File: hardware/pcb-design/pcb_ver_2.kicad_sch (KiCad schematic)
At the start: 28 parts, among them J1 GTFP08441BEU, J2 Conn_01x04_Pin, J3 USB4085-GF-A_REVA4, J4 Conn_01x07_Socket, J5 Screw_Terminal_01x02, J6 UART, Q1 NMOS, U1 ESP32-S3-WROOM-2, U2 LM1117MP-3.3

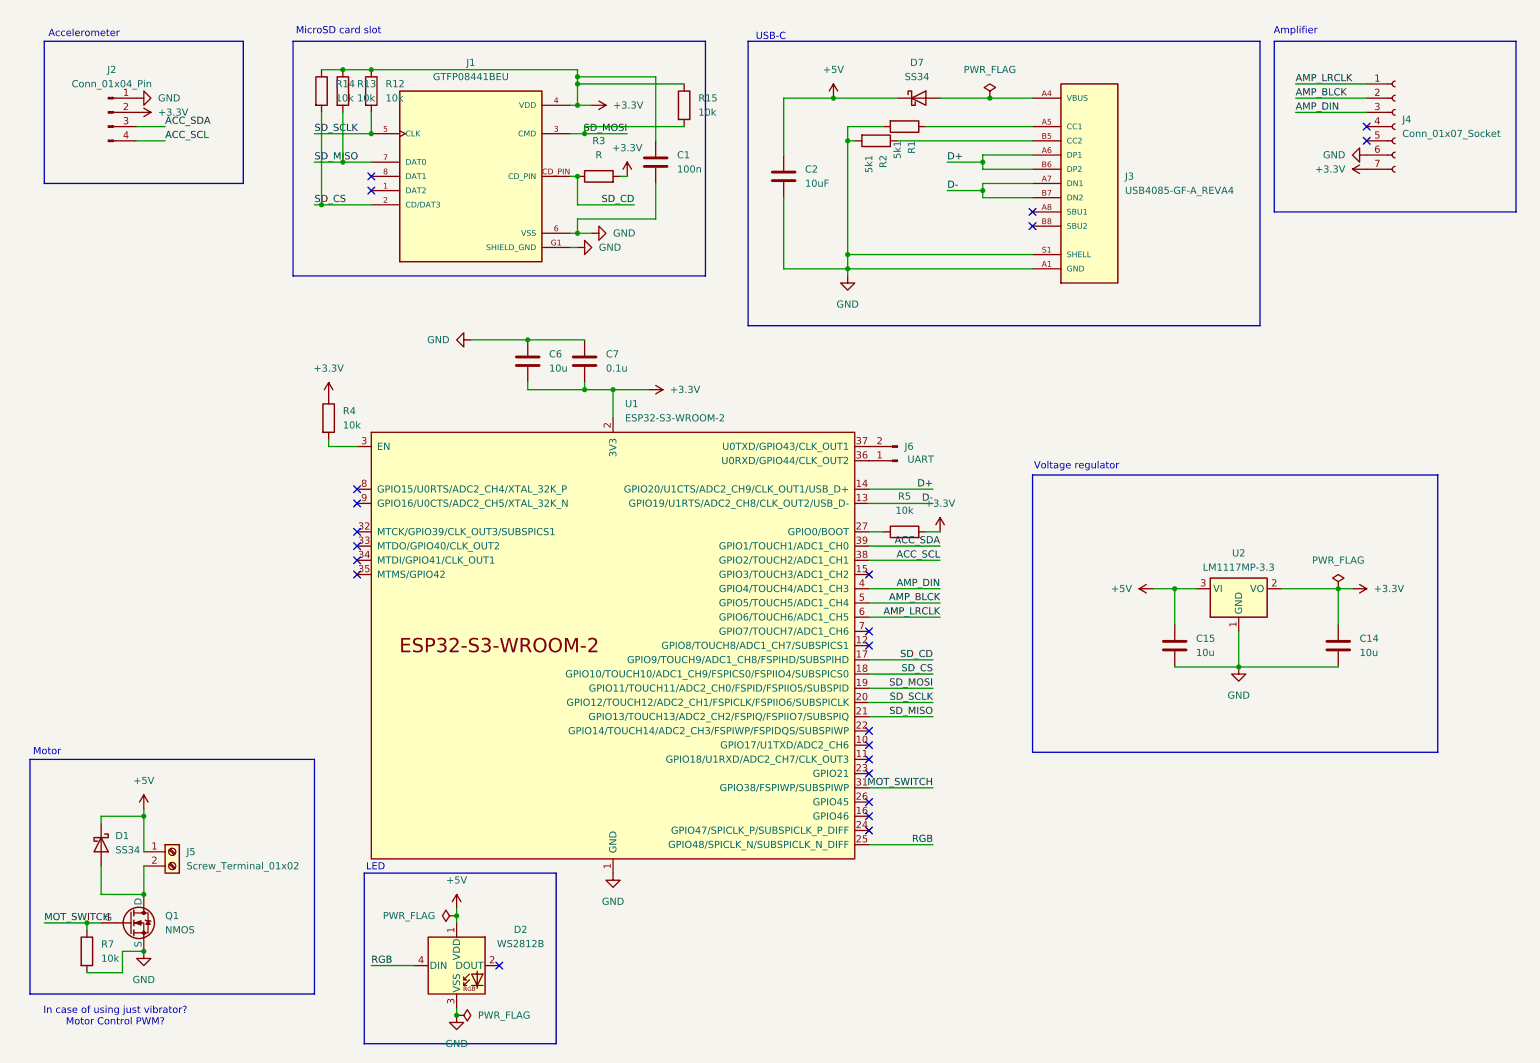
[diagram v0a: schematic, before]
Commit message: hardware: change to USB board
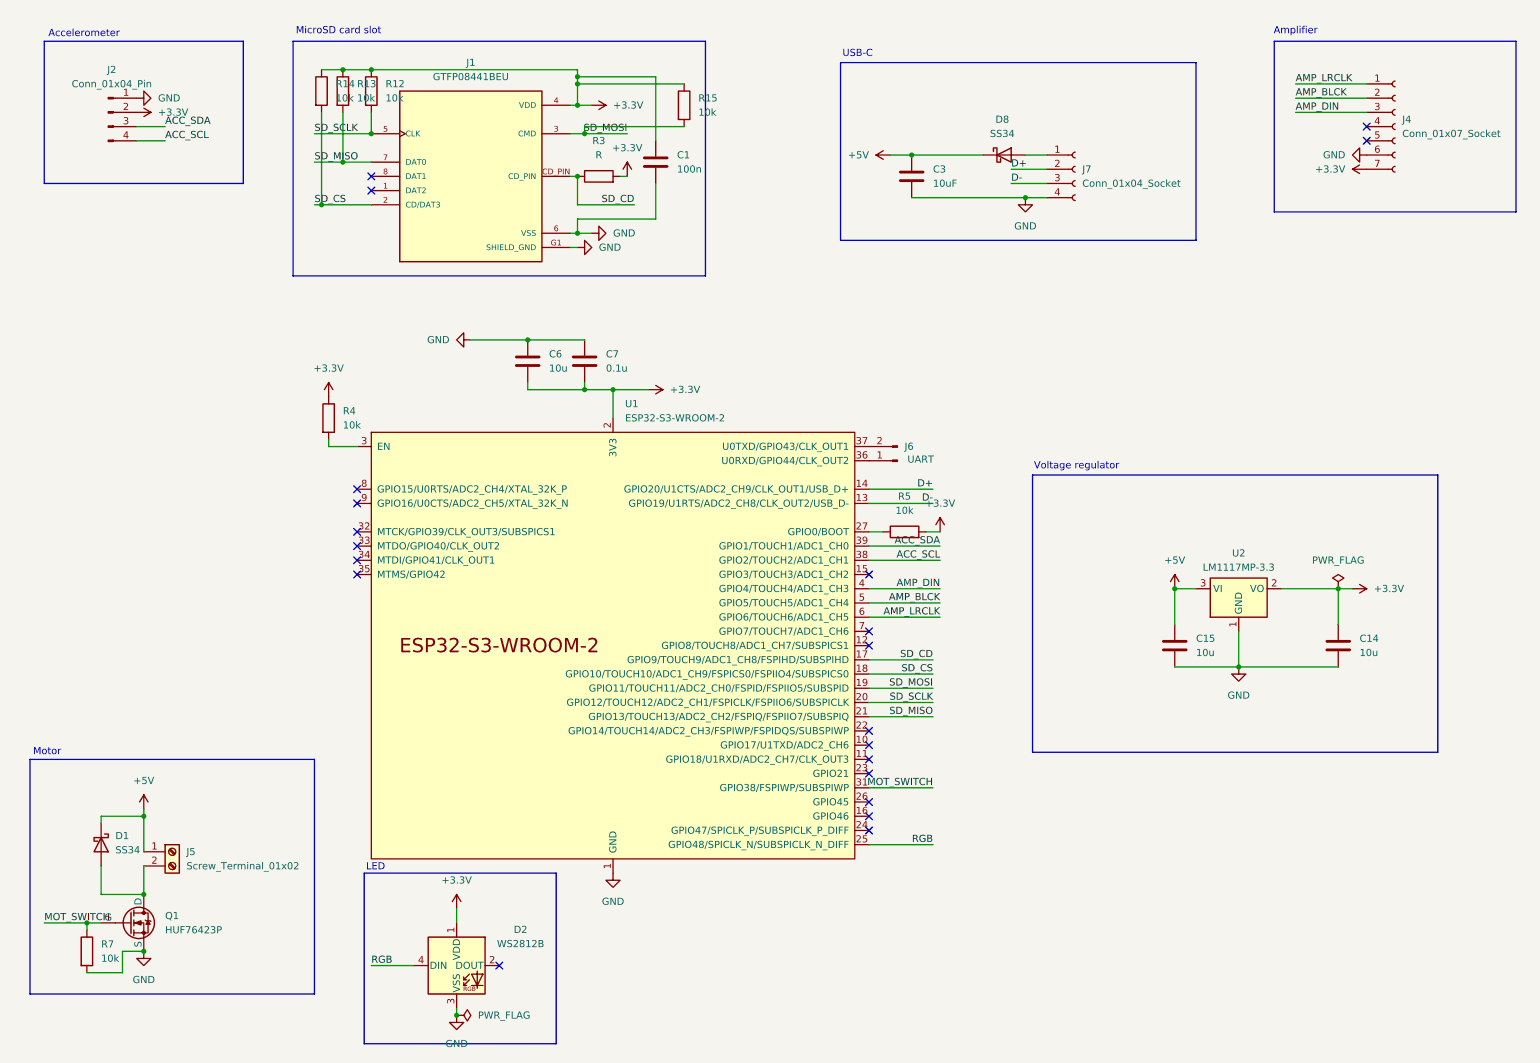
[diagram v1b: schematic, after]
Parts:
- removed C2: 10uF, Capacitor_Tantalum_SMD:CP_EIA-1608-10_AVX-L_HandSolder, symbol Device:C
- removed D7: SS34, Diode_SMD:D_SMA, symbol Diode:SS34
- removed J3: USB4085-GF-A_REVA4, USB4085-GF-A:GCT_USB4085-GF-A_REVA, symbol USB4085-GF-A_REVA4:USB4085-GF-A_REVA4
- removed R1, R2: 5k1, Resistor_SMD:R_0603_1608Metric_Pad0.98x0.95mm_HandSolder, symbol Device:R
- added C3: 10uF, Capacitor_Tantalum_SMD:CP_EIA-1608-10_AVX-L_HandSolder, symbol Device:C
- added D8: SS34, Diode_SMD:D_SMA, symbol Diode:SS34
- added J7: Conn_01x04_Socket, Connector:NS-Tech_Grove_1x04_P2mm_Vertical, symbol Connector:Conn_01x04_Socket
- Q1: value NMOS -> HUF76423P
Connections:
- net +3.3V: now also D2.1 (VDD)
- net +5V: now also C3.1, D8.1 (K); no longer D2.1 (VDD)
- net D+: now also J7.2 (Pin_2)
- net D-: now also J7.3 (Pin_3)
- net GND: now also C3.2, J7.4 (Pin_4)
- new net: D8.2 (A), J7.1 (Pin_1)
- no-connect marks 23 -> 21
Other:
- note removed: "In case of using just vibrator? Motor Control PWM?"

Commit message: hardware: remove vias and change sizes
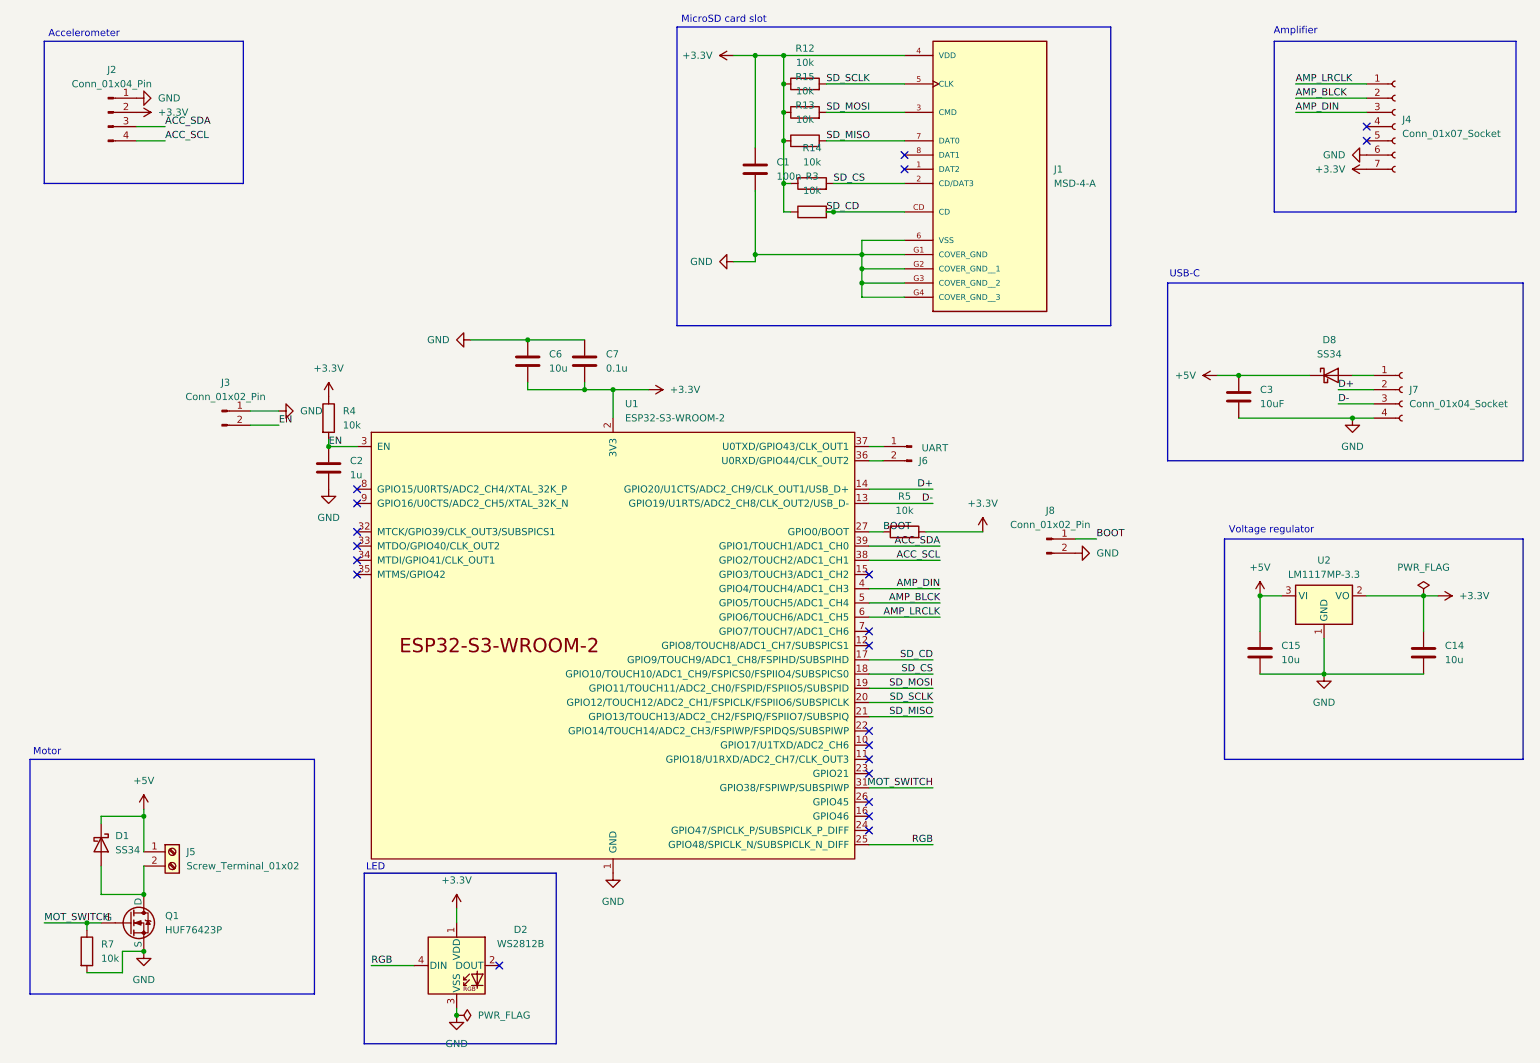
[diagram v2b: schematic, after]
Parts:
- removed J1: GTFP08441BEU, GTFP08441BEU:AMPHENOL_GTFP08441BEU, symbol GTFP08441BEU:GTFP08441BEU
- added C2: 1u, Capacitor_SMD:C_0603_1608Metric_Pad1.08x0.95mm_HandSolder, symbol Device:C
- added J1: MSD-4-A, MSD-4-A:CUI_MSD-4-A, symbol MSD-4-A:MSD-4-A
- added J3, J8: Conn_01x02_Pin, Connector_PinSocket_2.54mm:PinSocket_2x01_P2.54mm_Vertical, symbol Connector:Conn_01x02_Pin
- C1, C7: footprint Capacitor_Tantalum_SMD:CP_EIA-1608-10_AVX-L_HandSolder -> Capacitor_SMD:C_0603_1608Metric_Pad1.08x0.95mm_HandSolder
- C14, C15, C3, C6: footprint Capacitor_Tantalum_SMD:CP_EIA-1608-10_AVX-L_HandSolder -> Capacitor_SMD:C_0805_2012Metric_Pad1.18x1.45mm_HandSolder
- D1, D8: footprint Diode_SMD:D_SMA -> Diode_SMD:D_SMB-SMC_Universal_Handsoldering
- R3: value R -> 10k
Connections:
- net +3.3V: now also R3.1, J1.4 (VDD); no longer R3.2
- net GND: now also C2.2, J1.6 (VSS), J1.G1 (COVER_GND), J1.G2 (COVER_GND__1), J1.G3 (COVER_GND__2), J1.G4 (COVER_GND__3), J3.1 (Pin_1), J8.2 (Pin_2)
- net SD_CD: now also R3.2, J1.CD; no longer R3.1
- net SD_CS: now also J1.2 (CD/DAT3)
- net SD_MISO: now also J1.7 (DAT0)
- net SD_MOSI: now also J1.3 (CMD)
- net SD_SCLK: now also J1.5 (CLK)
- net at J6.1 (Pin_1): now also U1.37 (U0TXD/GPIO43/CLK_OUT1); no longer U1.36 (U0RXD/GPIO44/CLK_OUT2)
- net at J6.2 (Pin_2): now also U1.36 (U0RXD/GPIO44/CLK_OUT2); no longer U1.37 (U0TXD/GPIO43/CLK_OUT1)
- net EN: now reaches R4.2, U1.3 (EN)
- net EN: now also C2.1, J3.2 (Pin_2)
- net BOOT: now reaches R5.1, U1.27 (GPIO0/BOOT)
- net BOOT: now also J8.1 (Pin_1)
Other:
- moved on the sheet: C14, C15, C3, D8, J6, J7, U2
